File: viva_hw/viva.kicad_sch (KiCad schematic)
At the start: 30 parts, among them J1 Conn_01x05_Socket, J2 Conn_01x03_Socket, M1 XIAO_ESP32C3, Q1 NMOS, Q2 NMOS, Q3 NMOS, Q4 NMOS, U1 LM358, U2 LM358

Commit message: feat: began pcb work
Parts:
- added H1, H2, H3, H4: MountingHole_Pad, MountingHole:MountingHole_2.7mm_M2.5_DIN965_Pad, symbol Mechanical:MountingHole_Pad
- added J3: Battery, Connector_PinHeader_2.54mm:PinHeader_1x02_P2.54mm_Vertical, symbol Connector:Conn_01x02_Socket
- J1: value Conn_01x05_Socket -> Motor
- J2: value Conn_01x03_Socket -> EMG; footprint (none) -> Connector_PinHeader_2.54mm:PinHeader_1x03_P2.54mm_Vertical
- J4: renamed from ST7735; value Conn_01x08_Socket -> ST7735
- U2: footprint (none) -> Package_DIP:DIP-8_W7.62mm_Socket
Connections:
- net 0: now also R3.2, H1.1, H2.1, H3.1, H4.1, J3.2 (Pin_2)
- net at M1.16 (BAT+): no longer R3.2
- net at R4.2: now also J3.1 (Pin_1); no longer M1.15 (BAT-)
- no-connect marks 0 -> 3

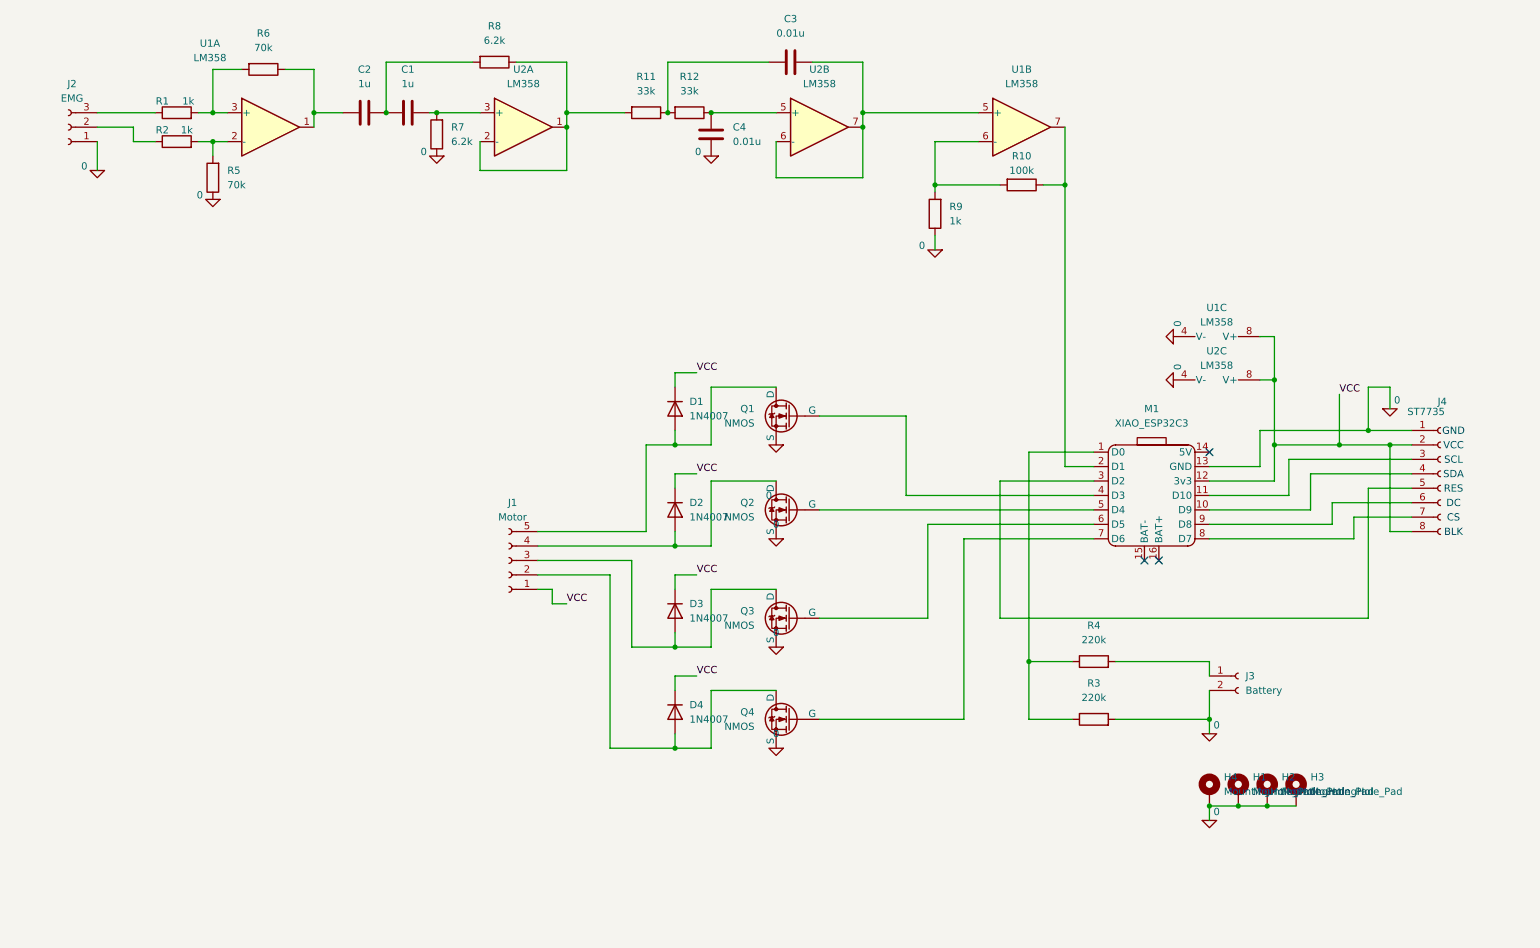
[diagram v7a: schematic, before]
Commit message: feat: added switches to schematic, created simulation sheet
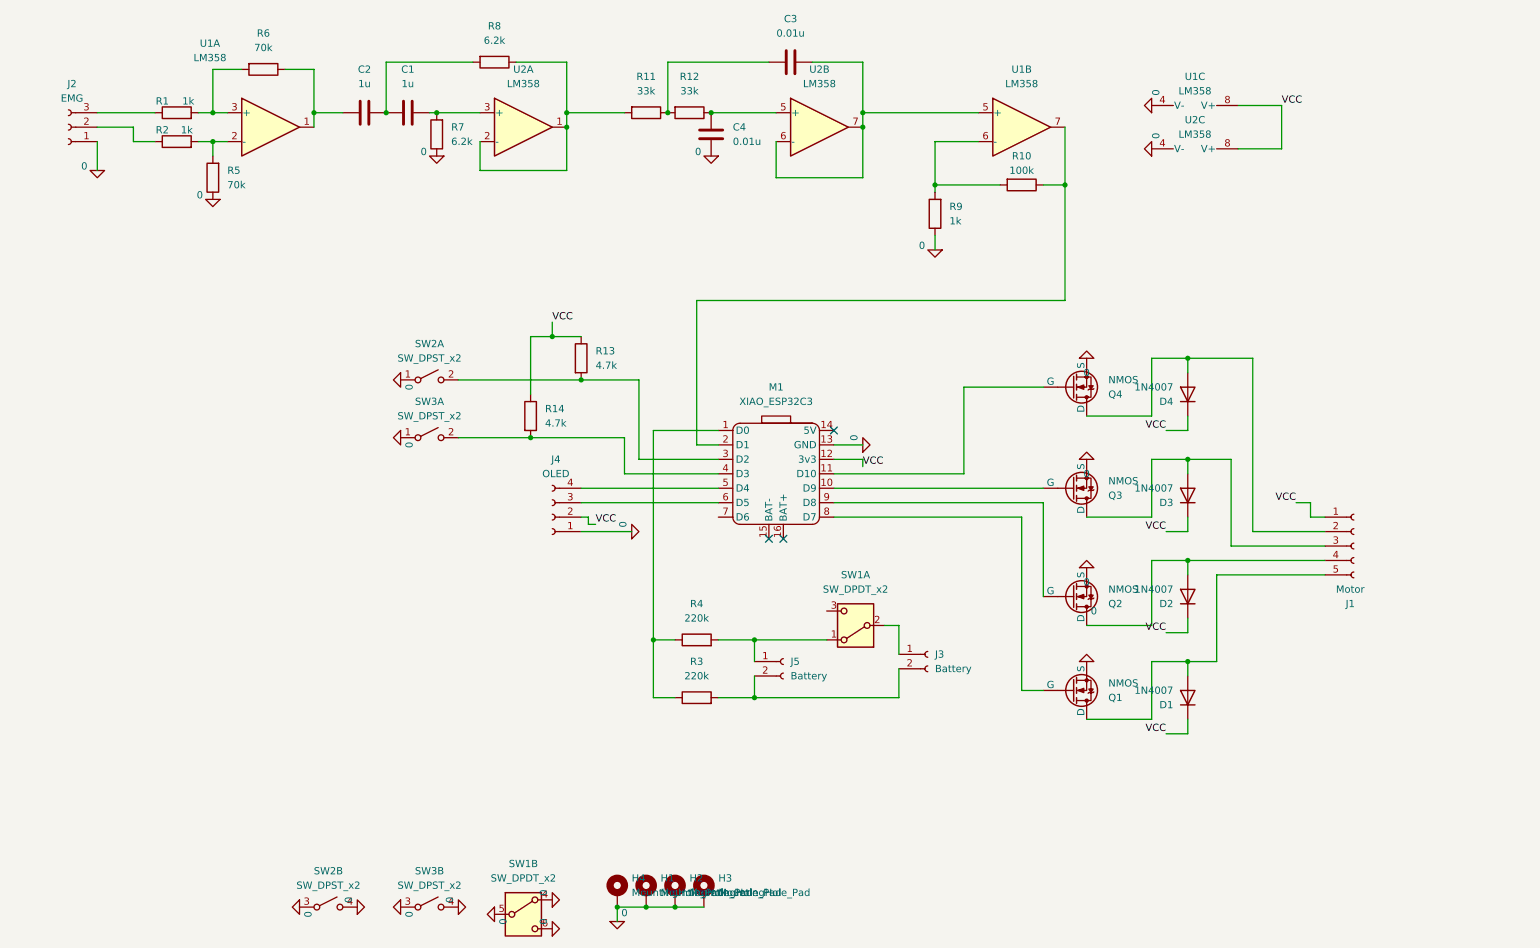
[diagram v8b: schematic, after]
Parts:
- removed J4: ST7735, Connector_PinHeader_2.54mm:PinHeader_1x08_P2.54mm_Vertical, symbol Connector:Conn_01x08_Socket
- added J4: OLED, symbol Connector:Conn_01x04_Socket
- added J5: Battery, Connector_PinHeader_2.54mm:PinHeader_1x02_P2.54mm_Vertical, symbol Connector:Conn_01x02_Socket
- added R13, R14: 4.7k, symbol Device:R
- added SW1: SW_DPDT_x2, symbol Switch:SW_DPDT_x2
- added SW2, SW3: SW_DPST_x2, symbol Switch:SW_DPST_x2
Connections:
- net 0: now also J4.1 (Pin_1), SW1.4 (A), SW1.5 (B), SW1.6 (C), SW2.1 (A), SW2.3 (A), SW2.4 (B), SW3.1 (A), SW3.3 (A), SW3.4 (B); no longer J3.2 (Pin_2), R3.2
- net VCC: now also J4.2 (Pin_2), R13.1, R14.1
- net at J3.1 (Pin_1): now also SW1.2 (B); no longer R4.2
- net at Q4.2 (G): now also M1.11 (D10); no longer M1.7 (D6)
- net at M1.6 (D5): now also J4.3 (Pin_3); no longer Q3.2 (G)
- net at M1.10 (D9): now also Q3.2 (G)
- net at M1.3 (D2): now also R13.2, SW2.2 (B)
- net at M1.4 (D3): now also R14.2, SW3.2 (B); no longer Q1.2 (G)
- net at M1.5 (D4): now also J4.4 (Pin_4); no longer Q2.2 (G)
- net at M1.8 (D7): now also Q1.2 (G)
- net at M1.9 (D8): now also Q2.2 (G)
- new net: J3.2 (Pin_2), J5.2 (Pin_2), R3.2
- new net: J5.1 (Pin_1), R4.2, SW1.1 (A)
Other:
- note removed: "BLK"
- note removed: "CS"
- note removed: "DC"
- note removed: "GND"
- note removed: "RES"
- note removed: "SCL"
- note removed: "SDA"
- note removed: "VCC"
- moved on the sheet: D1, D2, D3, D4, H1, H2, H3, H4, J1, J3, M1, Q1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
